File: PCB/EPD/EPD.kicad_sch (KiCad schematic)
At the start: 68 parts, among them J1 Conn_01x26, J2 Shelly, J3 USB-PROG, J4 BTN1, J6 BTN2, J7 USB-C-Socket-V, J8 PWR, P1 +, P10 2, P11 1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

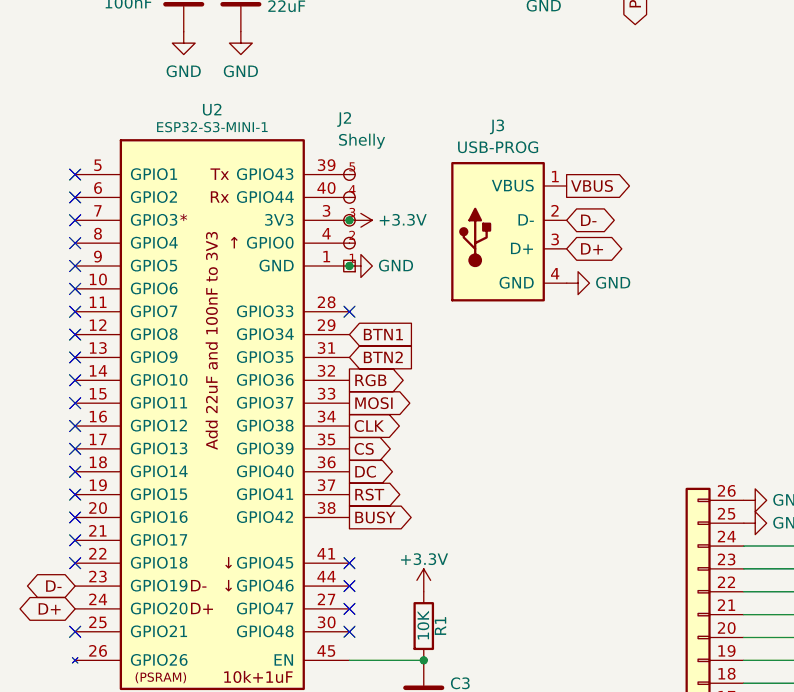
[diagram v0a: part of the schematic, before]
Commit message: Moved connector for less slack
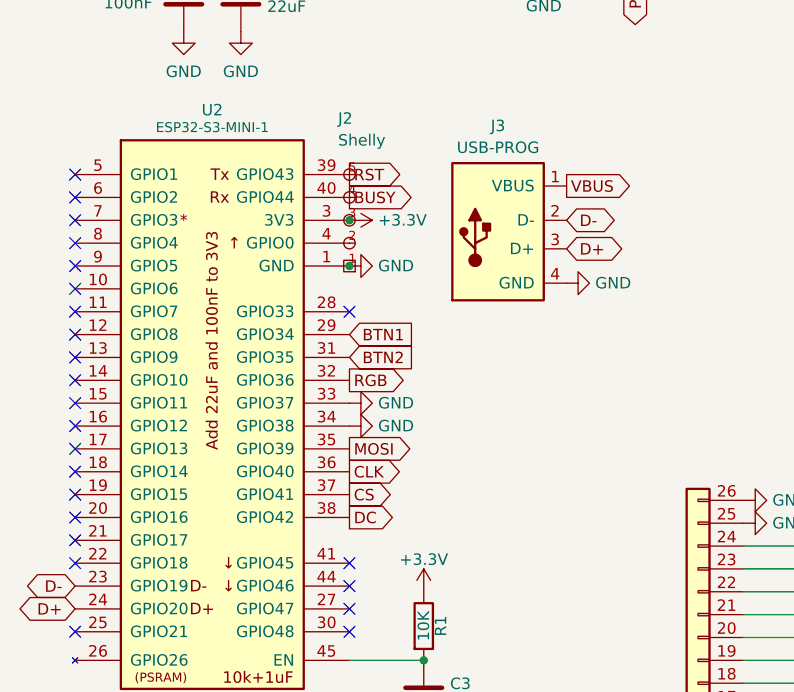
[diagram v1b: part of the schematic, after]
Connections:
- net BUSY: now also J2.4 (Rx), U2.40 (GPIO44); no longer U2.38 (GPIO42)
- net CLK: now also U2.36 (GPIO40); no longer U2.34 (GPIO38)
- net CS: now also U2.37 (GPIO41); no longer U2.35 (GPIO39)
- net DC: now also U2.38 (GPIO42); no longer U2.36 (GPIO40)
- net GND: now also U2.33 (GPIO37), U2.34 (GPIO38)
- net MOSI: now also U2.35 (GPIO39); no longer U2.33 (GPIO37)
- net RST: now also J2.5 (Tx), U2.39 (GPIO43); no longer U2.37 (GPIO41)
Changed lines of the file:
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@@
     )
   )
-  (global_label "MOSI" (shape output) (at 79.375 73.66 0) (fields_autoplaced)
-    (effects (font (size 1.27 1.27)) (justify left))
-    (property "Intersheetrefs" "${INTERSHEET_REFS}" (at 86.3022 73.66 0)
+  (global_label "MOSI" (shape output) (at 79.375 78.74 0) (fields_autoplaced)
+    (effects (font (size 1.27 1.27)) (justify left))
+    (property "Intersheetrefs" "${INTERSHEET_REFS}" (at 86.3022 78.74 0)
       (effects (font (size 1.27 1.27)) (justify left) hide)
     )
@@
     )
   )
-  (global_label "BUSY" (shape output) (at 79.375 86.36 0) (fields_autoplaced)
-    (effects (font (size 1.27 1.27)) (justify left))
-    (property "Intersheetrefs" "${INTERSHEET_REFS}" (at 86.6046 86.36 0)
+  (global_label "BUSY" (shape output) (at 79.375 50.8 0) (fields_autoplaced)
+    (effects (font (size 1.27 1.27)) (justify left))
+    (property "Intersheetrefs" "${INTERSHEET_REFS}" (at 86.6046 50.8 0)
       (effects (font (size 1.27 1.27)) (justify left) hide)
     )
@@
     )
   )
-  (global_label "DC" (shape output) (at 79.375 81.28 0) (fields_autoplaced)
-    (effects (font (size 1.27 1.27)) (justify left))
-    (property "Intersheetrefs" "${INTERSHEET_REFS}" (at 84.246 81.28 0)
+  (global_label "DC" (shape output) (at 79.375 86.36 0) (fields_autoplaced)
+    (effects (font (size 1.27 1.27)) (justify left))
+    (property "Intersheetrefs" "${INTERSHEET_REFS}" (at 84.246 86.36 0)
       (effects (font (size 1.27 1.27)) (justify left) hide)
     )
@@
     )
   )
-  (global_label "RST" (shape output) (at 79.375 83.82 0) (fields_autoplaced)
-    (effects (font (size 1.27 1.27)) (justify left))
-    (property "Intersheetrefs" "${INTERSHEET_REFS}" (at 85.1531 83.82 0)
-      (effects (font (size 1.27 1.27)) (justify left) hide)
-    )
-  )
-  (global_label "CS" (shape output) (at 79.375 78.74 0) (fields_autoplaced)
-    (effects (font (size 1.27 1.27)) (justify left))
-    (property "Intersheetrefs" "${INTERSHEET_REFS}" (at 84.1855 78.74 0)
+  (global_label "RST" (shape output) (at 79.375 48.26 0) (fields_autoplaced)
+    (effects (font (size 1.27 1.27)) (justify left))
+    (property "Intersheetrefs" "${INTERSHEET_REFS}" (at 85.1531 48.26 0)
+      (effects (font (size 1.27 1.27)) (justify left) hide)
+    )
+  )
+  (global_label "CS" (shape output) (at 79.375 83.82 0) (fields_autoplaced)
+    (effects (font (size 1.27 1.27)) (justify left))
+    (property "Intersheetrefs" "${INTERSHEET_REFS}" (at 84.1855 83.82 0)
       (effects (font (size 1.27 1.27)) (justify left) hide)
     )
@@
     )
   )
-  (global_label "CLK" (shape output) (at 79.375 76.2 0) (fields_autoplaced)
-    (effects (font (size 1.27 1.27)) (justify left))
-    (property "Intersheetrefs" "${INTERSHEET_REFS}" (at 85.2741 76.2 0)
+  (global_label "CLK" (shape output) (at 79.375 81.28 0) (fields_autoplaced)
+    (effects (font (size 1.27 1.27)) (justify left))
+    (property "Intersheetrefs" "${INTERSHEET_REFS}" (at 85.2741 81.28 0)
       (effects (font (size 1.27 1.27)) (justify left) hide)
     )
@@
         (path "/46c350bb-7de4-4e81-aafd-4af55e37aab0"
           (reference "JP2") (unit 1)
+        )
+      )
+    )
+  )
+  (symbol (lib_id "power:GND") (at 79.375 73.66 90) (unit 1)
+    (in_bom yes) (on_board yes) (dnp no) (fields_autoplaced)
+    (property "Reference" "#PWR0105" (at 85.725 73.66 0)
+      (effects (font (size 1.27 1.27)) hide)
+    )
+    (property "Value" "GND" (at 82.55 73.66 90)
+      (effects (font (size 1.27 1.27)) (justify right))
+    )
+    (property "Footprint" "" (at 79.375 73.66 0)
+      (effects (font (size 1.27 1.27)) hide)
+    )
+    (property "Datasheet" "" (at 79.375 73.66 0)
+      (effects (font (size 1.27 1.27)) hide)
+    )
+    (pin "1")
+    (instances
+      (project "USBA"
+        (path "/2d210a96-f81f-42a9-8bf4-1b43c11086f3"
+          (reference "#PWR0105") (unit 1)
+        )
+      )
+      (project "EPD"
+        (path "/46c350bb-7de4-4e81-aafd-4af55e37aab0"
+          (reference "#PWR021") (unit 1)
         )
       )
@@
         )
       )
+    )
+  )
+  (symbol (lib_id "power:GND") (at 79.375 76.2 90) (unit 1)
+    (in_bom yes) (on_board yes) (dnp no) (fields_autoplaced)
+    (property "Reference" "#PWR0105" (at 85.725 76.2 0)
+      (effects (font (size 1.27 1.27)) hide)
+    )
+    (property "Value" "GND" (at 82.55 76.2 90)
+      (effects (font (size 1.27 1.27)) (justify right))
+    )
+    (property "Footprint" "" (at 79.375 76.2 0)
+      (effects (font (size 1.27 1.27)) hide)
+    )
+    (property "Datasheet" "" (at 79.375 76.2 0)
+      (effects (font (size 1.27 1.27)) hide)
+    )
+    (pin "1")
+    (instances
+      (project "USBA"
+        (path "/2d210a96-f81f-42a9-8bf4-1b43c11086f3"
+          (reference "#PWR0105") (unit 1)
+        )
+      )
+      (project "EPD"
+        (path "/46c350bb-7de4-4e81-aafd-4af55e37aab0"
+          (reference "#PWR022") (unit 1)
+        )
+      )

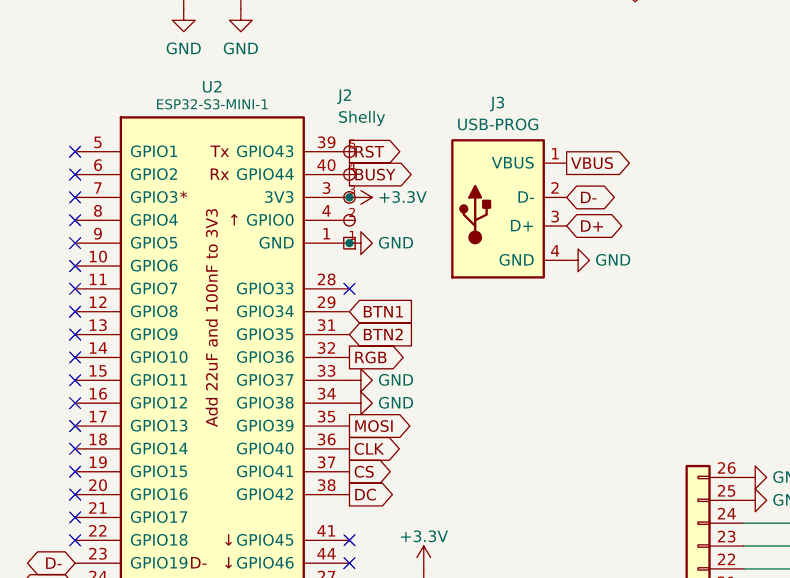
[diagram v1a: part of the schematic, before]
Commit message: Moved connector and tidy GPIOs used
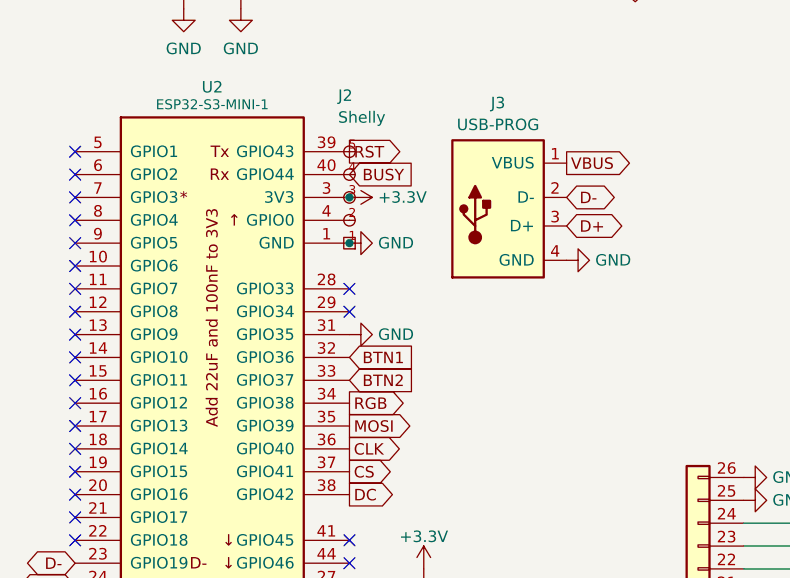
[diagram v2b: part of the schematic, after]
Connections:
- net BTN1: now also U2.32 (GPIO36); no longer U2.29 (GPIO34)
- net BTN2: now also U2.33 (GPIO37); no longer U2.31 (GPIO35)
- net GND: now also U2.31 (GPIO35); no longer U2.33 (GPIO37), U2.34 (GPIO38)
- net RGB: now also U2.34 (GPIO38); no longer U2.32 (GPIO36)
- no-connect marks 29 -> 30
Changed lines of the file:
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@@
   (no_connect (at 123.19 132.715))
   (no_connect (at 48.895 68.58))
+  (no_connect (at 79.375 66.04))
   (no_connect (at 48.895 58.42))
   (no_connect (at 79.375 93.98))
@@
     )
   )
-  (global_label "BTN2" (shape input) (at 79.375 68.58 0) (fields_autoplaced)
-    (effects (font (size 1.27 1.27)) (justify left))
-    (property "Intersheetrefs" "${INTERSHEET_REFS}" (at 86.4836 68.58 0)
+  (global_label "BTN2" (shape input) (at 79.375 73.66 0) (fields_autoplaced)
+    (effects (font (size 1.27 1.27)) (justify left))
+    (property "Intersheetrefs" "${INTERSHEET_REFS}" (at 86.4836 73.66 0)
       (effects (font (size 1.27 1.27)) (justify left) hide)
     )
@@
     )
   )
-  (global_label "BUSY" (shape output) (at 79.375 50.8 0) (fields_autoplaced)
+  (global_label "BUSY" (shape input) (at 79.375 50.8 0) (fields_autoplaced)
     (effects (font (size 1.27 1.27)) (justify left))
     (property "Intersheetrefs" "${INTERSHEET_REFS}" (at 86.6046 50.8 0)
@@
     )
   )
-  (global_label "RGB" (shape output) (at 79.375 71.12 0) (fields_autoplaced)
-    (effects (font (size 1.27 1.27)) (justify left))
-    (property "Intersheetrefs" "${INTERSHEET_REFS}" (at 85.516 71.12 0)
+  (global_label "RGB" (shape output) (at 79.375 76.2 0) (fields_autoplaced)
+    (effects (font (size 1.27 1.27)) (justify left))
+    (property "Intersheetrefs" "${INTERSHEET_REFS}" (at 85.516 76.2 0)
       (effects (font (size 1.27 1.27)) (justify left) hide)
     )
@@
     )
   )
-  (global_label "BTN1" (shape input) (at 79.375 66.04 0) (fields_autoplaced)
-    (effects (font (size 1.27 1.27)) (justify left))
-    (property "Intersheetrefs" "${INTERSHEET_REFS}" (at 86.4836 66.04 0)
+  (global_label "BTN1" (shape input) (at 79.375 71.12 0) (fields_autoplaced)
+    (effects (font (size 1.27 1.27)) (justify left))
+    (property "Intersheetrefs" "${INTERSHEET_REFS}" (at 86.4836 71.12 0)
       (effects (font (size 1.27 1.27)) (justify left) hide)
     )
@@
     )
   )
+  (symbol (lib_id "power:GND") (at 79.375 68.58 90) (unit 1)
+    (in_bom yes) (on_board yes) (dnp no) (fields_autoplaced)
+    (property "Reference" "#PWR01" (at 85.725 68.58 0)
+      (effects (font (size 1.27 1.27)) hide)
+    )
+    (property "Value" "GND" (at 82.55 68.58 90)
+      (effects (font (size 1.27 1.27)) (justify right))
+    )
+    (property "Footprint" "" (at 79.375 68.58 0)
+      (effects (font (size 1.27 1.27)) hide)
+    )
+    (property "Datasheet" "" (at 79.375 68.58 0)
+      (effects (font (size 1.27 1.27)) hide)
+    )
+    (pin "1")
+    (instances
+      (project "USBA"
+        (path "/2d210a96-f81f-42a9-8bf4-1b43c11086f3"
+          (reference "#PWR01") (unit 1)
+        )
+      )
+      (project "EPD"
+        (path "/46c350bb-7de4-4e81-aafd-4af55e37aab0"
+          (reference "#PWR021") (unit 1)
+        )
+      )
+    )
+  )
   (symbol (lib_id "power:+3.3V") (at 189.865 100.33 270) (unit 1)
     (in_bom yes) (on_board yes) (dnp no) (fields_autoplaced)
@@
         (path "/46c350bb-7de4-4e81-aafd-4af55e37aab0"
           (reference "JP2") (unit 1)
-        )
-      )
-    )
-  )
-  (symbol (lib_id "power:GND") (at 79.375 73.66 90) (unit 1)
-    (in_bom yes) (on_board yes) (dnp no) (fields_autoplaced)
-    (property "Reference" "#PWR0105" (at 85.725 73.66 0)
-      (effects (font (size 1.27 1.27)) hide)
-    )
-    (property "Value" "GND" (at 82.55 73.66 90)
-      (effects (font (size 1.27 1.27)) (justify right))
-    )
-    (property "Footprint" "" (at 79.375 73.66 0)
-      (effects (font (size 1.27 1.27)) hide)
-    )
-    (property "Datasheet" "" (at 79.375 73.66 0)
-      (effects (font (size 1.27 1.27)) hide)
-    )
-    (pin "1")
-    (instances
-      (project "USBA"
-        (path "/2d210a96-f81f-42a9-8bf4-1b43c11086f3"
-          (reference "#PWR0105") (unit 1)
-        )
-      )
-      (project "EPD"
-        (path "/46c350bb-7de4-4e81-aafd-4af55e37aab0"
-          (reference "#PWR021") (unit 1)
         )
       )
@@
         )
       )
-    )
-  )
-  (symbol (lib_id "power:GND") (at 79.375 76.2 90) (unit 1)
-    (in_bom yes) (on_board yes) (dnp no) (fields_autoplaced)
-    (property "Reference" "#PWR0105" (at 85.725 76.2 0)
-      (effects (font (size 1.27 1.27)) hide)
-    )
-    (property "Value" "GND" (at 82.55 76.2 90)
-      (effects (font (size 1.27 1.27)) (justify right))
-    )
-    (property "Footprint" "" (at 79.375 76.2 0)
-      (effects (font (size 1.27 1.27)) hide)
-    )
-    (property "Datasheet" "" (at 79.375 76.2 0)
-      (effects (font (size 1.27 1.27)) hide)
-    )
-    (pin "1")
-    (instances
-      (project "USBA"
-        (path "/2d210a96-f81f-42a9-8bf4-1b43c11086f3"
-          (reference "#PWR0105") (unit 1)
-        )
-      )
-      (project "EPD"
-        (path "/46c350bb-7de4-4e81-aafd-4af55e37aab0"
-          (reference "#PWR022") (unit 1)
-        )
-      )

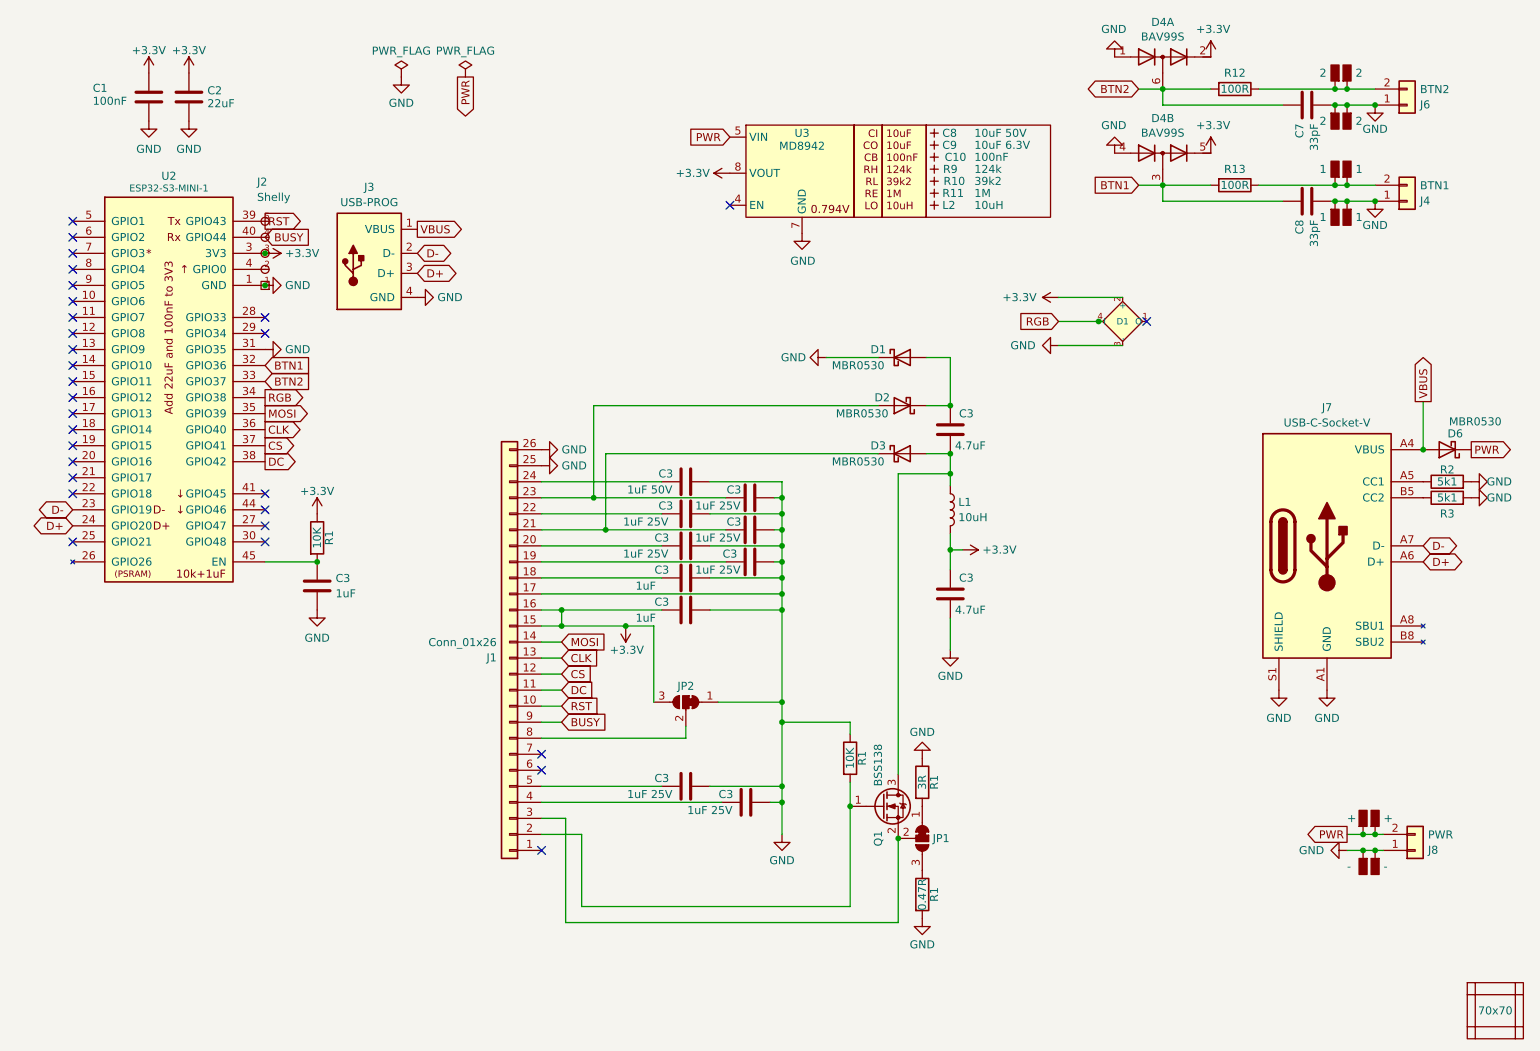
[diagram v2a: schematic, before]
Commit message: Changed ESD
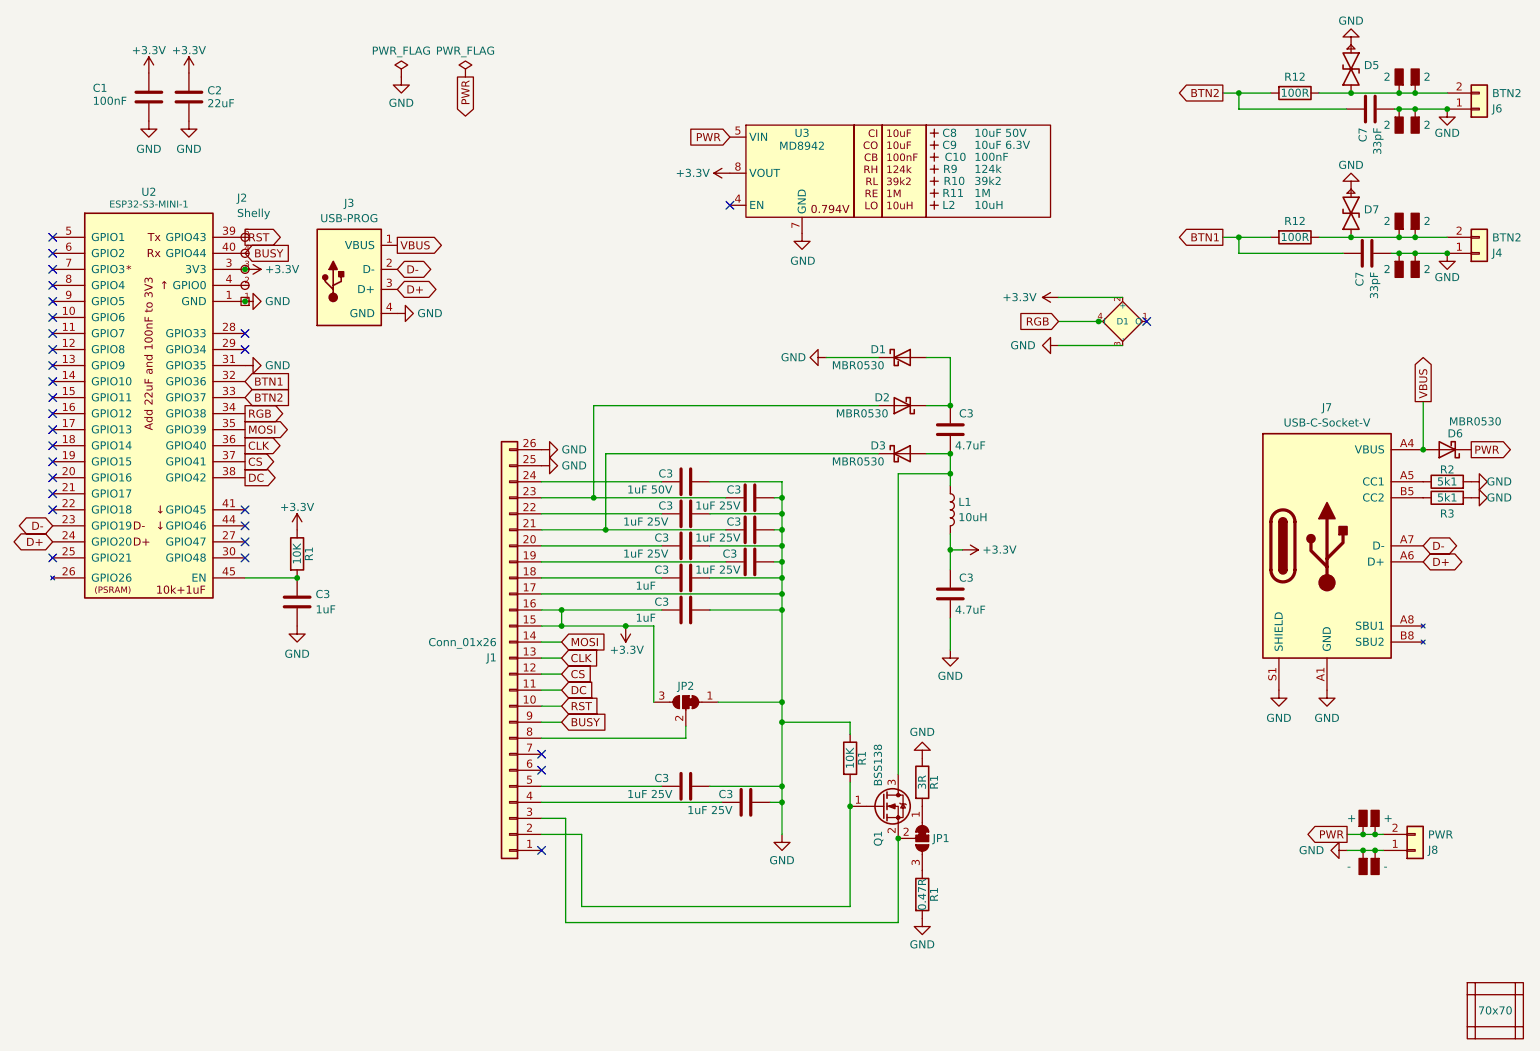
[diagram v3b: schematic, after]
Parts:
- removed C8: 33pF, RevK:C_0402, symbol Device:C
- removed D4: BAV99S, RevK:SOT-363_SC-70-6, symbol Diode:BAV99S
- removed R13: 100R, RevK:R_0402, symbol Device:R
- added C7: 33pF, RevK:C_0402, symbol Device:C
- added D5, D7: ~, RevK:DFN1006-2L, symbol RevK:ES05D1MC10
- added R12: 100R, RevK:R_0402, symbol Device:R
- J4: value BTN1 -> BTN2
- P11, P12, P5, P6: value 1 -> 2
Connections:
- net BTN1: now also C7.1, R12.2
- net GND: now also C7.2, D5.1, D7.1
- net at J6.2 (Pin_2), P3.1 (P), P9.1 (P)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: now also D5.2
- net at J4.2 (Pin_2), P11.1 (P), P5.1 (P): now also D7.2, R12.1
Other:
- moved on the sheet: C3, C7, J2, J3, J6, R1, R12, U2
